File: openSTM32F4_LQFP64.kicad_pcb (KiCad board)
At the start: 2 copper layers, 54 x 68 mm, 77 parts, among them J1 Jack-DC, J10 Conn_01x04, J11 Conn_01x04, J12 Conn_01x05, J13 USB_B_Micro, J14 Conn_01x04, J15 Conn_01x04, J16 Conn_01x05, J17 Conn_01x06, J18 Conn_01x04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

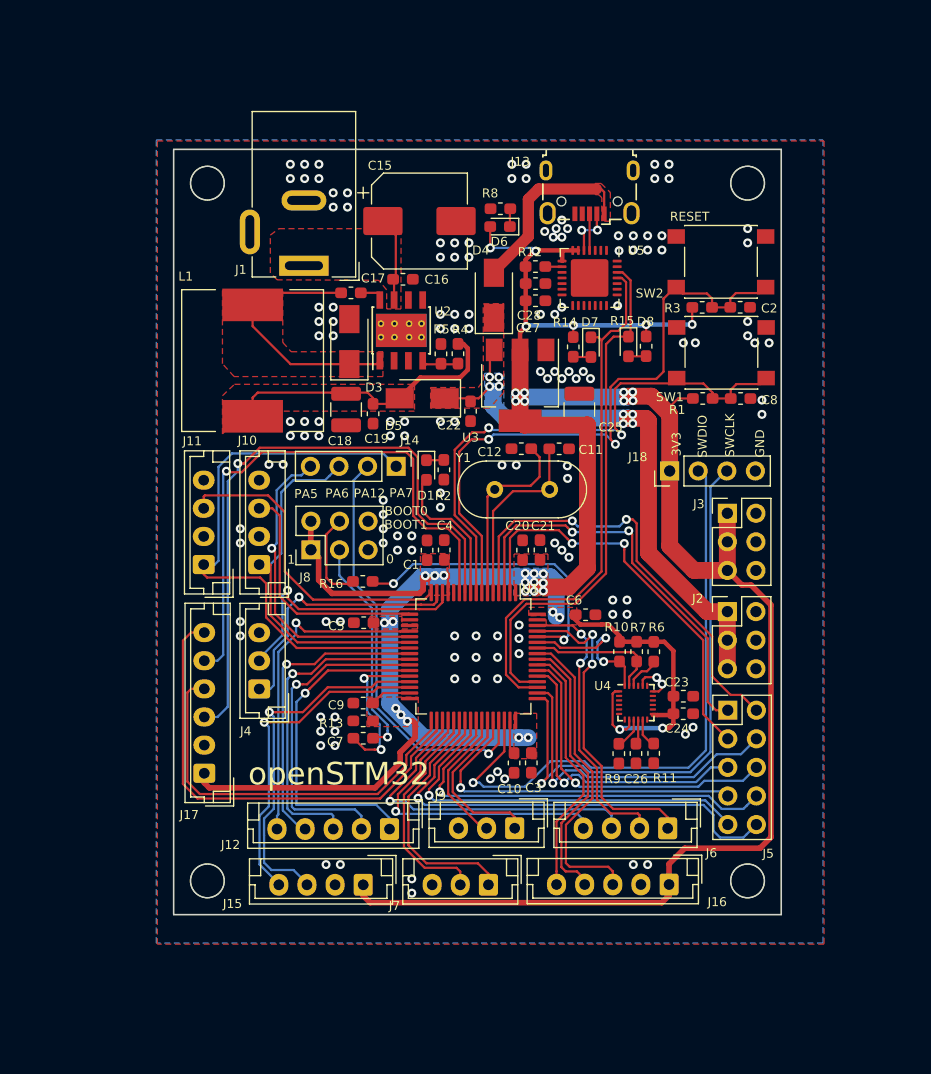
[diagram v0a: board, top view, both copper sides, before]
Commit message: update gnd via
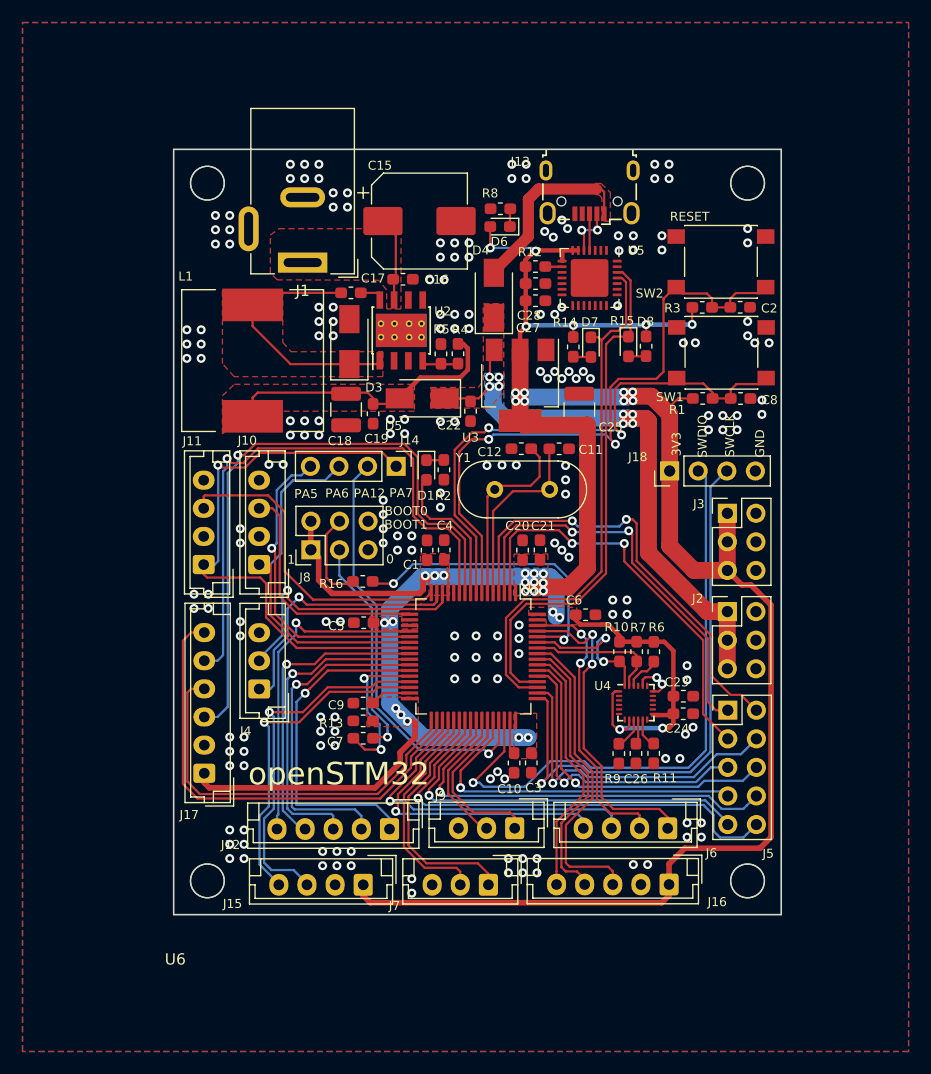
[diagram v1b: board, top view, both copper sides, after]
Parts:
- J1: value Jack-DC -> Barrel_Jack_Switch
- U6: footprint footprints:openstm_outline -> footprints:openSTM32F4_LQFP64_outline
- moved J1 0.30 mm to (151.2, 51.7)
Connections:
- J1 pad 3: (no net) -> GND
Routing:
- net I2S2_SD: track 50.7 -> 51.8 mm
- net I2S2_EXT_SD: track 56.3 -> 57.0 mm
- net MOTOR_RIGHT_PULSE: track 50.2 -> 50.6 mm, vias 0 -> 1
- net GND: vias 144 -> 196
